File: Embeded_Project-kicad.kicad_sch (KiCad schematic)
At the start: 0 parts

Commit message: temporary placement of an arduino and BME280
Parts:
- added A1: Arduino_Nano_v2.x, Module:Arduino_Nano, symbol MCU_Module:Arduino_Nano_v2.x
- added U1: BME280, Package_LGA:Bosch_LGA-8_2.5x2.5mm_P0.65mm_ClockwisePinNumbering, symbol Sensor:BME280
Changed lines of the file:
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@@
 	(generator_version "10.0")
 	(paper "A4")
+	(symbol
+		(lib_id "MCU_Module:Arduino_Nano_v2.x")
+		(at 185.42 90.17 0)
+		(unit 1)
+		(body_style 1)
+		(exclude_from_sim no)
+		(in_bom yes)
+		(on_board yes)
+		(in_pos_files yes)
+		(dnp no)
+		(fields_autoplaced yes)
+		(property "Reference" "A1"
+			(at 190.1033 115.57 0)
+			(show_name no)
+			(do_not_autoplace no)
+			(effects
+				(font
+					(size 1.27 1.27)
+				)
+				(justify left)
+			)
+		)
+		(property "Value" "Arduino_Nano_v2.x"
+			(at 190.1033 118.11 0)
+			(show_name no)
+			(do_not_autoplace no)
+			(effects
+				(font
+					(size 1.27 1.27)
+				)
+				(justify left)
+			)
+		)
+		(property "Footprint" "Module:Arduino_Nano"
+			(at 185.42 90.17 0)
+			(hide yes)
+			(show_name no)
+			(do_not_autoplace no)
+			(effects
+				(font
+					(size 1.27 1.27)
+					(italic yes)
+				)
+			)
+		)
+		(property "Datasheet" "https://www.arduino.cc/en/uploads/Main/ArduinoNanoManual23.pdf"
+			(at 185.42 90.17 0)
+			(hide yes)
+			(show_name no)
+			(do_not_autoplace no)
+			(effects
+				(font
+					(size 1.27 1.27)
+				)
+			)
+		)
+		(property "Description" "Arduino Nano v2.x"
+			(at 185.42 90.17 0)
+			(hide yes)
+			(show_name no)
+			(do_not_autoplace no)
+			(effects
+				(font
+					(size 1.27 1.27)
+				)
+			)
+		)
+		(pin "22"
+		)
+		(pin "23"
+		)
+		(pin "24"
+		)
+		(pin "25"
+		)
+		(pin "26"
+		)
+		(pin "27"
+		)
+		(pin "28"
+		)
+		(pin "29"
+		)
+		(pin "30"
+		)
+		(pin "10"
+		)
+		(pin "11"
+		)
+		(pin "12"
+		)
+		(pin "13"
+		)
+		(pin "14"
+		)
+		(pin "15"
+		)
+		(pin "16"
+		)
+		(pin "17"
+		)
+		(pin "18"
+		)
+		(pin "19"
+		)
+		(pin "20"
+		)
+		(pin "21"
+		)
+		(pin "1"
+		)
+		(pin "2"
+		)
+		(pin "3"
+		)
+		(pin "4"
+		)
+		(pin "5"
+		)
+		(pin "6"
+		)
+		(pin "7"
+		)
+		(pin "8"
+		)
+		(pin "9"
+		)
+		(instances
+			(project "Embeded_Project-kicad"
+				(path "/e7299fe2-e9b0-4d85-8fe7-9e0667a9cf19"
+					(reference "A1")
+					(unit 1)
+				)
+			)
+		)
+	)
+	(symbol
+		(lib_id "Sensor:BME280")
+		(at 86.36 81.28 0)
+		(unit 1)
+		(body_style 1)
+		(exclude_from_sim no)
+		(in_bom yes)
+		(on_board yes)
+		(in_pos_files yes)
+		(dnp no)
+		(fields_autoplaced yes)
+		(property "Reference" "U1"
+			(at 74.93 80.0099 0)
+			(show_name no)
+			(do_not_autoplace no)
+			(effects
+				(font
+					(size 1.27 1.27)
+				)
+				(justify right)
+			)
+		)
+		(property "Value" "BME280"
+			(at 74.93 82.5499 0)
+			(show_name no)
+			(do_not_autoplace no)
+			(effects
+				(font
+					(size 1.27 1.27)
+				)
+				(justify right)
+			)
+		)
+		(property "Footprint" "Package_LGA:Bosch_LGA-8_2.5x2.5mm_P0.65mm_ClockwisePinNumbering"
+			(at 124.46 92.71 0)
+			(hide yes)
+			(show_name no)
+			(do_not_autoplace no)
+			(effects
+				(font
+					(size 1.27 1.27)
+				)
+			)
+		)
+		(property "Datasheet" "https://www.bosch-sensortec.com/media/boschsensortec/downloads/datasheets/bst-bme280-ds002.pdf"
+			(at 86.36 86.36 0)
+			(hide yes)
+			(show_name no)
+			(do_not_autoplace no)
+			(effects
+				(font
+					(size 1.27 1.27)
+				)
+			)
+		)
+		(property "Description" "3-in-1 sensor, humidity, pressure, temperature, I2C and SPI interface, 1.71-3.6V, LGA-8"
+			(at 86.36 81.28 0)
+			(hide yes)
+			(show_name no)
+			(do_not_autoplace no)
+			(effects
+				(font
+					(size 1.27 1.27)
+				)
+			)
+		)
+		(pin "8"
+		)
+		(pin "7"
+		)
+		(pin "6"
+		)
+		(pin "5"
+		)
+		(pin "4"
+		)
+		(pin "3"
+		)
+		(pin "2"
+		)
+		(pin "1"
+		)
+		(instances
+			(project "Embeded_Project-kicad"
+				(path "/e7299fe2-e9b0-4d85-8fe7-9e0667a9cf19"
+					(reference "U1")
+					(unit 1)
+				)
+			)
+		)
+	)
 	(sheet_instances
 		(path "/"

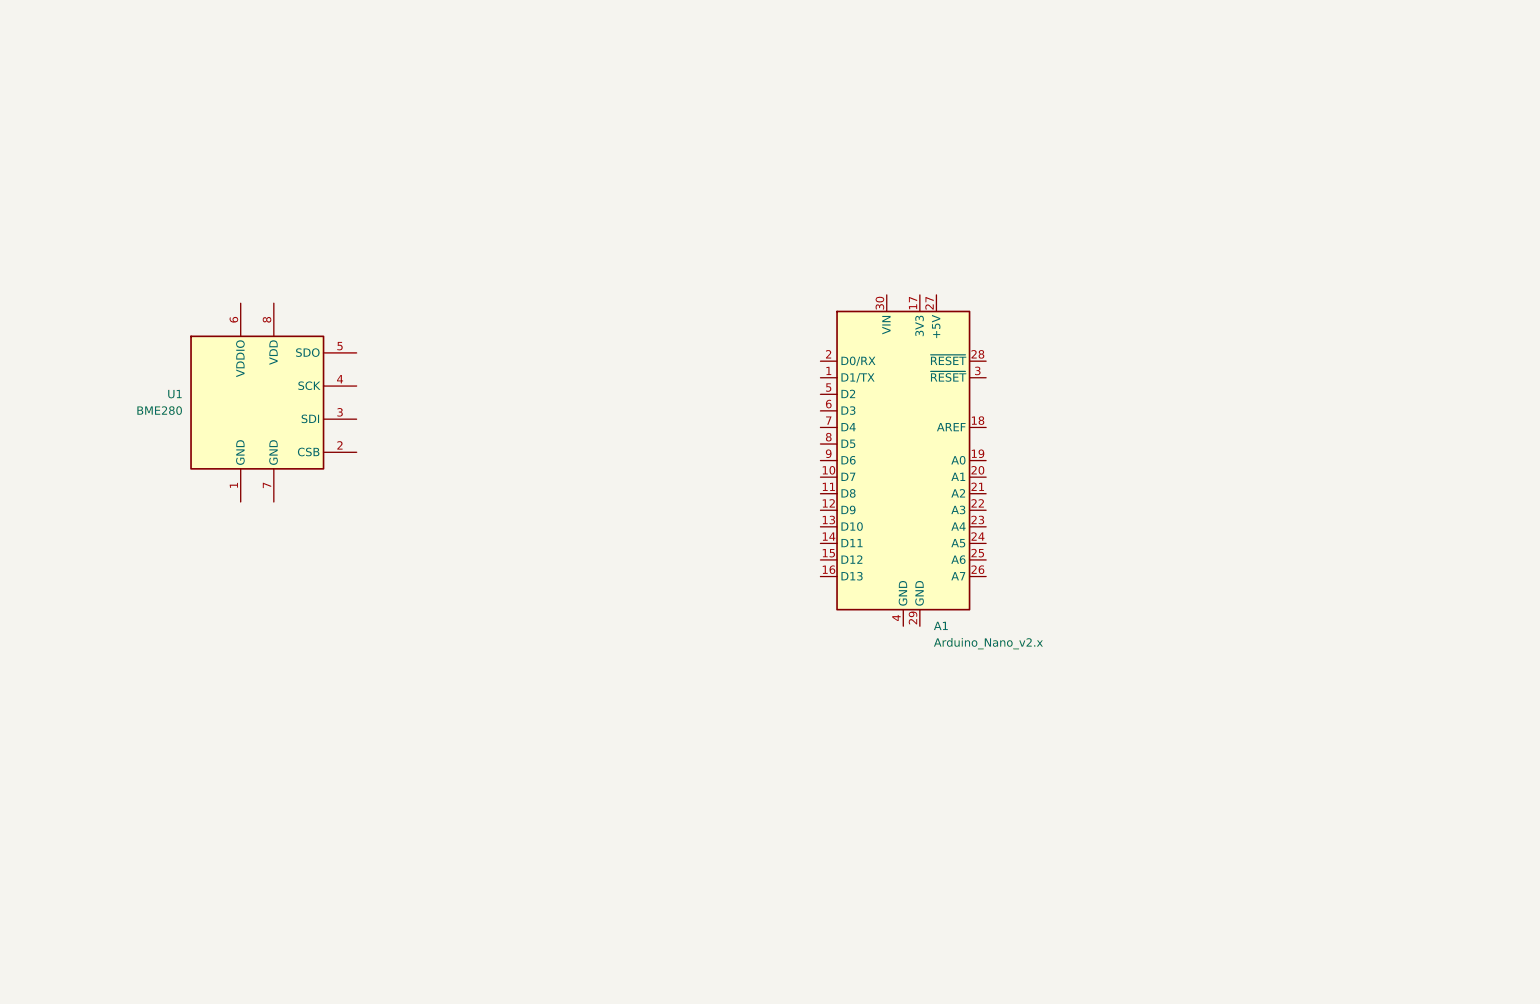
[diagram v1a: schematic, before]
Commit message: Initial rough sensor board schematic
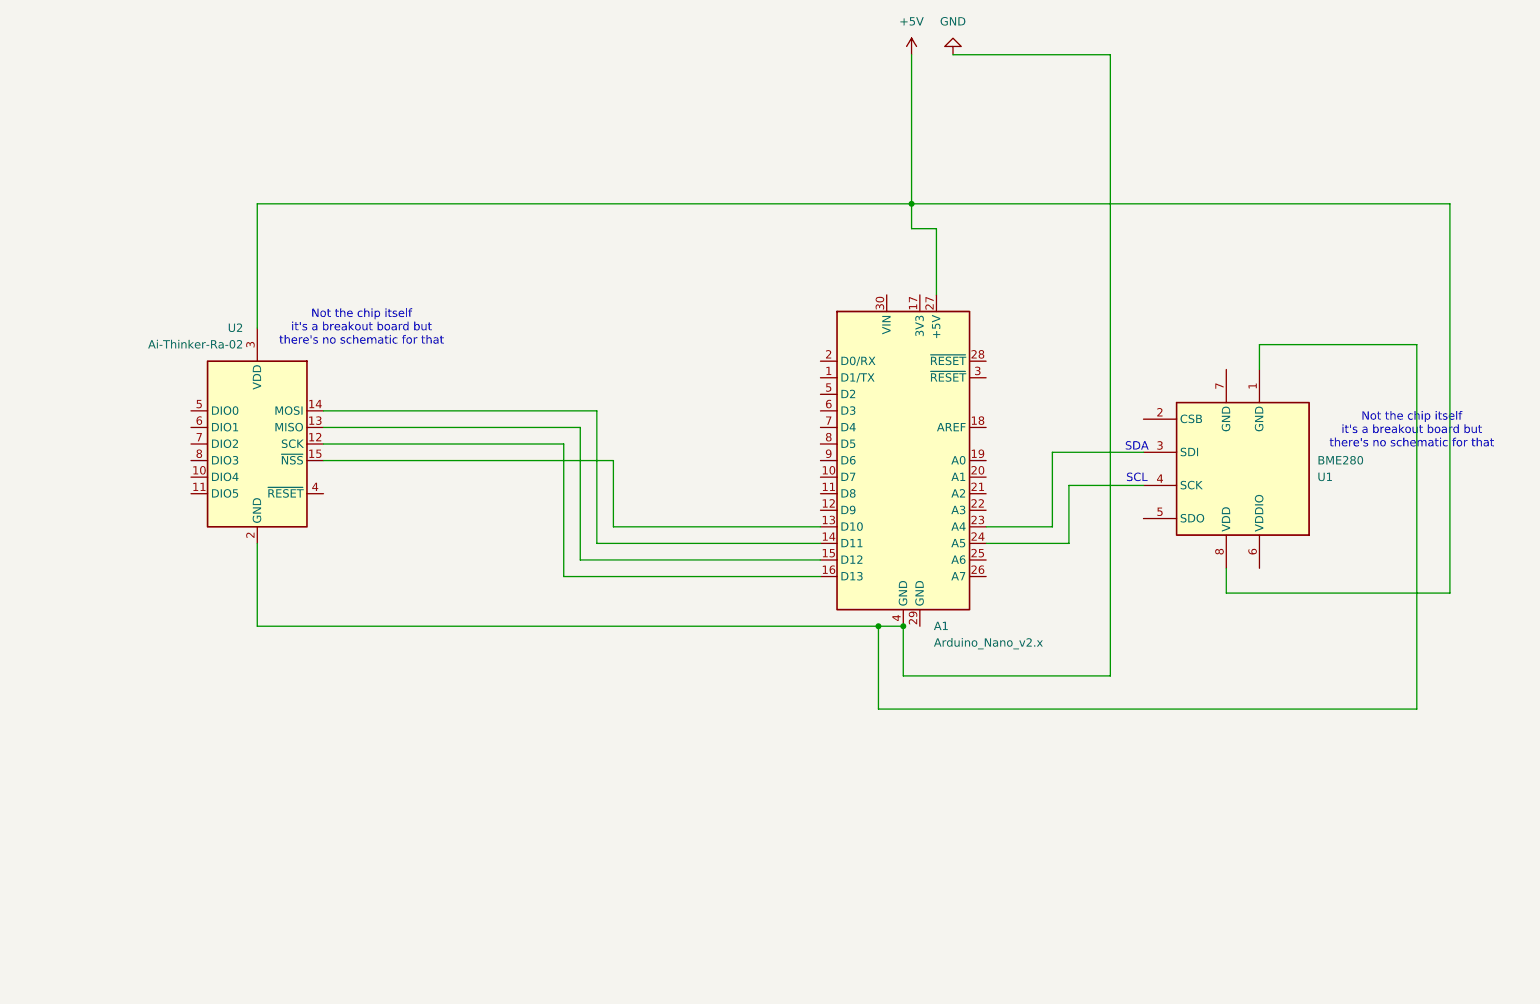
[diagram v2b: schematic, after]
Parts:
- added U2: Ai-Thinker-Ra-02, RF_Module:Ai-Thinker-Ra-01-LoRa, symbol RF_Module:Ai-Thinker-Ra-02
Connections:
- net at A1.13 (D10): now also U2.15 (~{NSS})
- net at A1.14 (D11): now also U2.14 (MOSI)
- net at A1.15 (D12): now also U2.13 (MISO)
- net at A1.16 (D13): now also U2.12 (SCK)
- net at A1.23 (A4): now also U1.3 (SDI)
- net at A1.24 (A5): now also U1.4 (SCK)
- net +5V: now reaches A1.27 (+5V)
- net +5V: now also U1.8 (VDD), U2.3 (VDD)
- net GND: now reaches A1.4 (GND)
- net GND: now also U1.1 (GND), U2.1 (GND), U2.16 (GND), U2.2 (GND), U2.9 (GND)
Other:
- note added: "Not the chip itself it's a breakout board but there's no schematic for that"
- note added: "SCL"
- note added: "SDA"
- title: (none) -> Sensor board rough schematic

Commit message: Fix: voltage fix for LoRa circuit
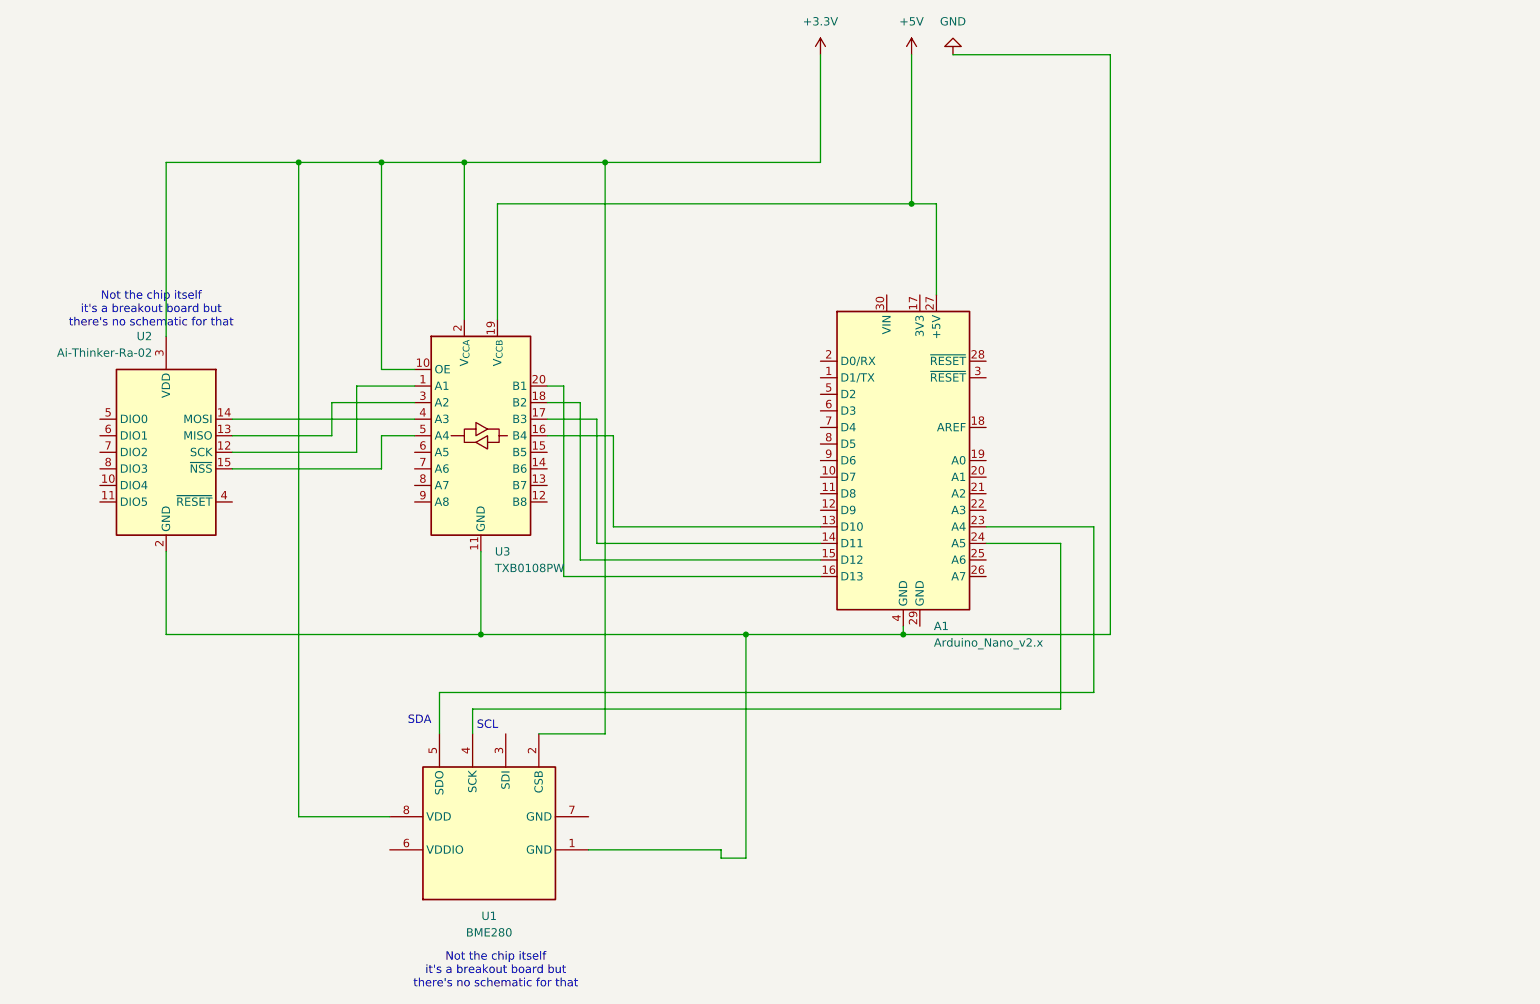
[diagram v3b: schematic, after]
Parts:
- added U3: TXB0108PW, Package_SO:TSSOP-20_4.4x6.5mm_P0.65mm, symbol Logic_LevelTranslator:TXB0108PW
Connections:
- net +5V: now also U3.19 (V_{CCB}); no longer U1.8 (VDD), U2.3 (VDD)
- net GND: now also U3.11 (GND)
- net at U2.12 (SCK): now also U3.1 (A1); no longer A1.16 (D13)
- net at A1.15 (D12): now also U3.18 (B2); no longer U2.13 (MISO)
- net at A1.14 (D11): now also U3.17 (B3); no longer U2.14 (MOSI)
- net at A1.13 (D10): now also U3.16 (B4); no longer U2.15 (~{NSS})
- net +3.3V: now reaches U1.2 (CSB)
- net +3.3V: now also U1.8 (VDD), U2.3 (VDD), U3.10 (OE), U3.2 (V_{CCA})
- net at U1.3 (SDI): no longer A1.23 (A4)
- net at U1.5 (SDO): now also A1.23 (A4)
- new net: A1.16 (D13), U3.20 (B1)
- new net: U2.13 (MISO), U3.3 (A2)
- new net: U2.14 (MOSI), U3.4 (A3)
- new net: U2.15 (~{NSS}), U3.5 (A4)
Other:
- moved on the sheet: U1, U2
